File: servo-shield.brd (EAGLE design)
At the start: 65 x 56 mm, 31 parts, among them K1 PIN20X2

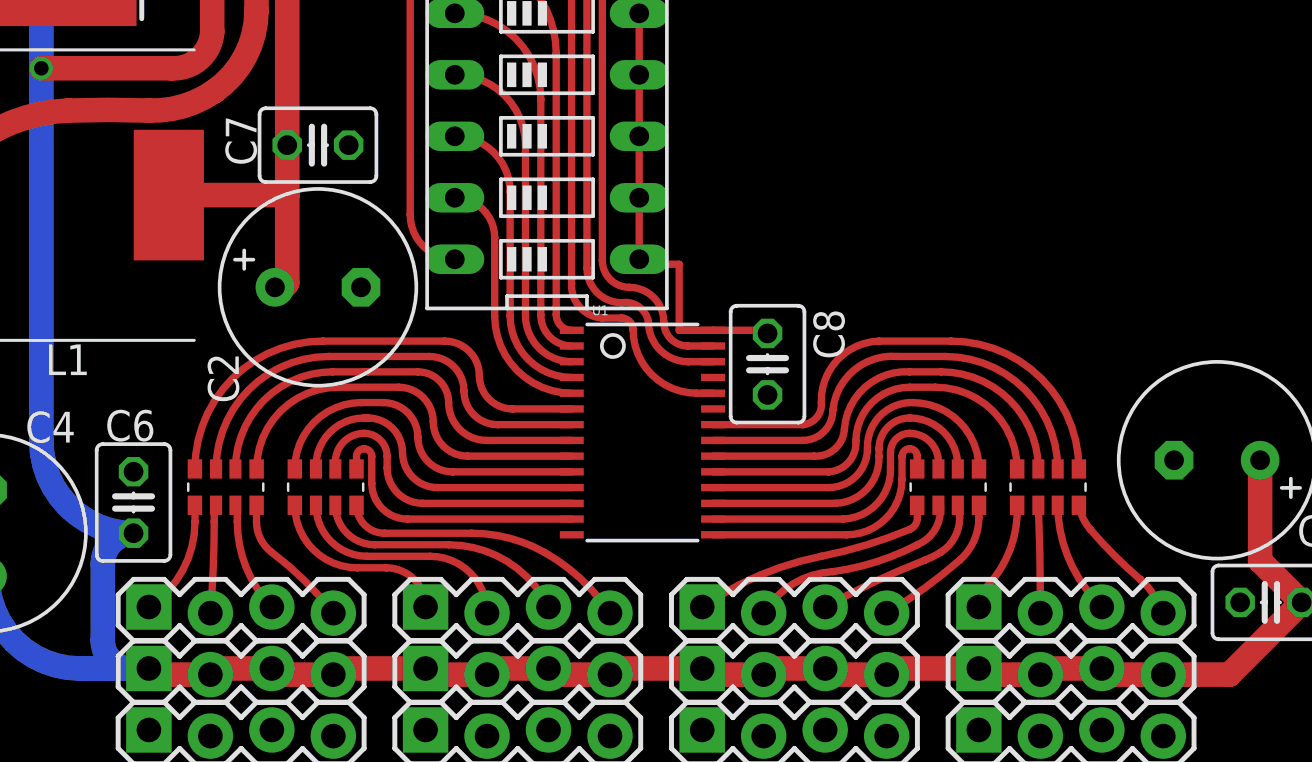
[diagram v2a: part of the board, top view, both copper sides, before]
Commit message: Rejig location of resistor networks
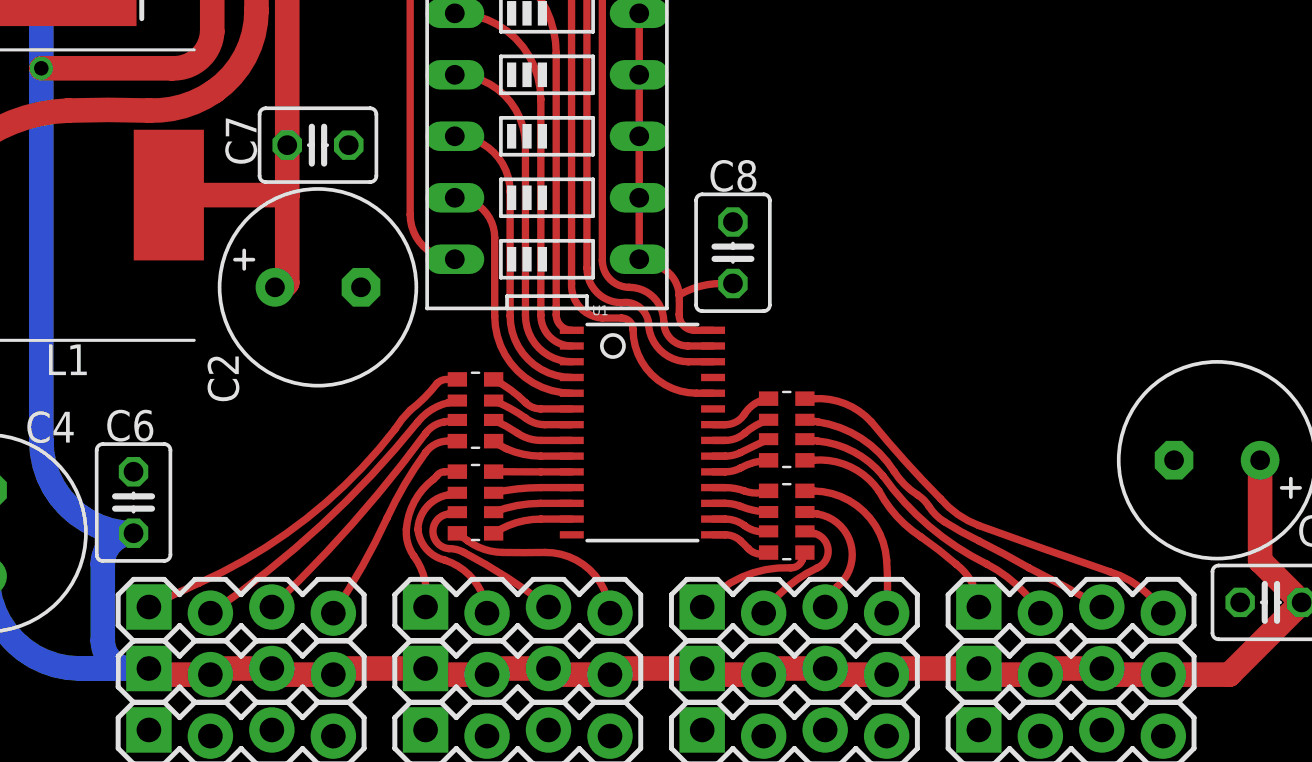
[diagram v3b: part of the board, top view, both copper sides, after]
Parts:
- moved RN1 11.1 mm to (37.8, 15.1), turned to 270 degrees
- moved RN4 10.8 mm to (24.9, 15.9), turned to 90 degrees
- moved RN2 6.82 mm to (37.8, 11.3), turned to 270 degrees
- moved RN3 6.22 mm to (24.9, 12.1), turned to 90 degrees
- moved C8 4.82 mm to (35.6, 22.4), turned to 90 degrees
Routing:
- net N$23: track 18.8 -> 2.59 mm
- net N$35: track 18.9 -> 3.59 mm
- net N$24: track 17.5 -> 2.49 mm
- net N$34: track 17.8 -> 3.46 mm
- net N$25: track 16.4 -> 2.44 mm
- net N$33: track 16.7 -> 3.42 mm
- net N$26: track 15.5 -> 2.36 mm
- net N$32: track 15.6 -> 3.35 mm
- net N$22: track 5.72 -> 17.7 mm
- net N$8: track 4.69 -> 16.0 mm
- net N$27: track 13.6 -> 2.31 mm
- net N$31: track 13.8 -> 3.23 mm
- net N$28: track 12.8 -> 2.33 mm
- net N$21: track 4.61 -> 14.6 mm
- net N$1: track 12.0 -> 2.37 mm
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
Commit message: Adding EagleCAD logo
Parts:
- added U$1: (no value), logo:EAGLE-PLC-8MM
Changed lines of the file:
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@@
 <attribute name="VALUE" x="13.843" y="9.779" size="1.27" layer="27" ratio="10" rot="R90"/>
 </element>
+<element name="U$1" library="logo" package="EAGLE-PLC-8MM" value="" x="40.16375" y="9.04875"/>
 </elements>
 <signals>

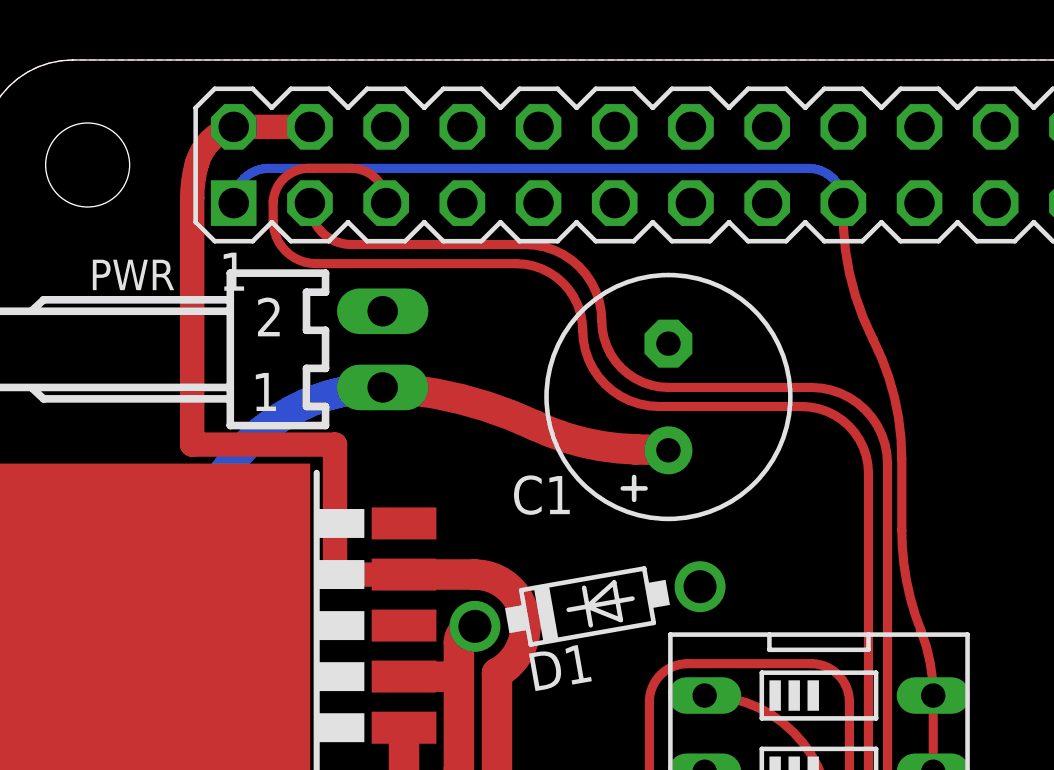
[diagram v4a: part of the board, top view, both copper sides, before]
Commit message: add jumper to select if RaspberryPi uses servo board regulator.
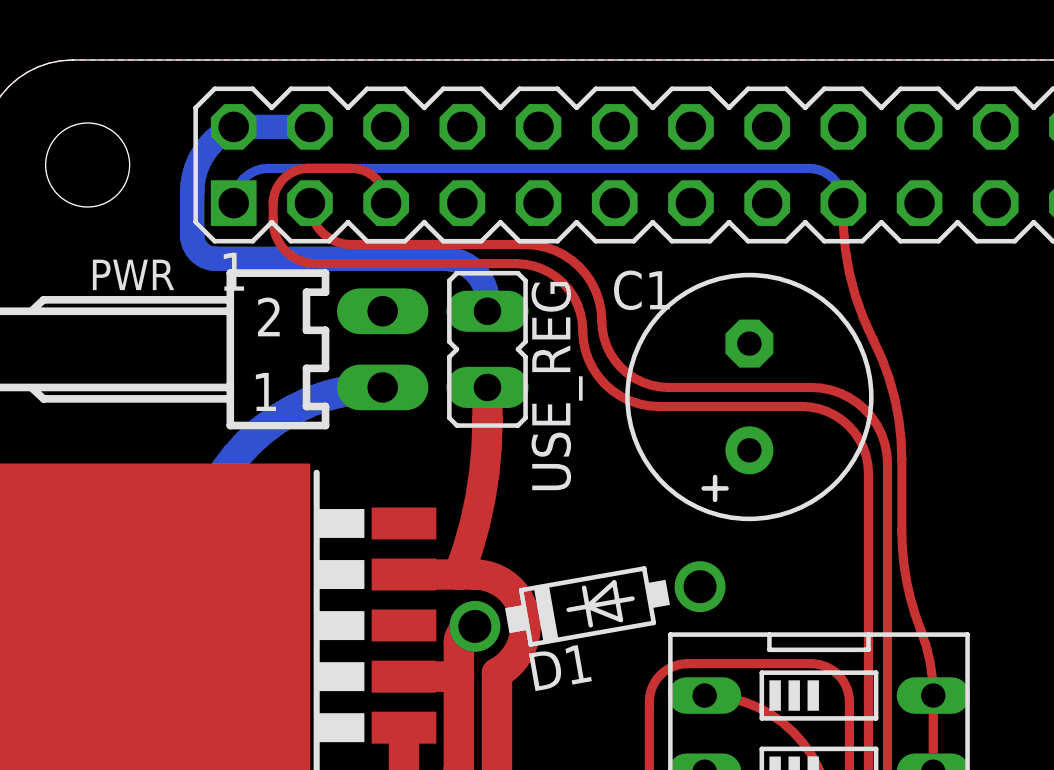
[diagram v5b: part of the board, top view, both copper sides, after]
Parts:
- added USE_REG: (no value), jumper:JP1
- moved C1 2.70 mm to (25.6, 44.8)
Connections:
- new net N$16: K1.2, K1.4, USE_REG.2
- net +5V: now also USE_REG.1; no longer K1.2, K1.4
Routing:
- net +5V: track 51.5 -> 32.8 mm
- net N$16: track 0.00 -> 17.6 mm
- net V+: track 130.9 -> 121.1 mm
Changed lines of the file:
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@@
 <attribute name="VALUE" x="16.129" y="23.78075" size="1.27" layer="27" ratio="10"/>
 </element>
-<element name="C1" library="rcl" package="E3,5-8" value="1000uf" x="22.86" y="44.7675" smashed="yes" rot="R90">
-<attribute name="NAME" x="19.71675" y="42.13225" size="1.27" layer="25" ratio="10" rot="R180"/>
-<attribute name="VALUE" x="25.908" y="42.4815" size="1.27" layer="27" ratio="10" rot="R90"/>
+<element name="C1" library="rcl" package="E3,5-8" value="1000uf" x="25.55875" y="44.7675" smashed="yes" rot="R90">
+<attribute name="NAME" x="23.0505" y="48.9585" size="1.27" layer="25" ratio="10" rot="R180"/>
+<attribute name="VALUE" x="28.60675" y="42.4815" size="1.27" layer="27" ratio="10" rot="R90"/>
 </element>
 <element name="C8" library="rcl" package="C025-030X050" value="100nf" x="35.56" y="22.38375" smashed="yes" rot="R90">
@@
 </element>
 <element name="U$1" library="logo" package="EAGLE-PLC-8MM" value="" x="40.16375" y="9.04875"/>
+<element name="USE_REG" library="jumper" package="JP1" value="" x="16.8275" y="46.355" smashed="yes">
+<attribute name="NAME" x="18.31975" y="48.73625" size="1.27" layer="25" ratio="10" rot="R270"/>
+<attribute name="VALUE" x="19.7485" y="43.815" size="1.27" layer="27" ratio="10" rot="R90"/>
+</element>
 </elements>
 <signals>
@@
 </signal>
 <signal name="+5V">
-<contactref element="K1" pad="2"/>
-<contactref element="K1" pad="4"/>
 <contactref element="IC2" pad="4"/>
 <contactref element="L1" pad="2"/>
@@
 <wire x1="17.145" y1="24.765" x2="17.145" y2="26.82875" width="1.016" layer="1"/>
 <wire x1="12.2525" y1="24.765" x2="17.145" y2="24.765" width="1.016" layer="1"/>
-<wire x1="14.0462" y1="38.8493" x2="11.7475" y2="38.8493" width="0.8128" layer="1"/>
-<wire x1="11.7475" y1="38.8493" x2="11.7475" y2="43.18" width="0.8128" layer="1"/>
-<wire x1="11.7475" y1="43.18" x2="6.985" y2="43.18" width="0.8128" layer="1"/>
-<wire x1="6.985" y1="43.18" x2="6.985" y2="51.38875" width="0.8128" layer="1"/>
-<wire x1="10.91" y1="53.77" x2="8.37" y2="53.77" width="0.8128" layer="1"/>
-<wire x1="14.0462" y1="38.8493" x2="16.3957" y2="38.8493" width="1.016" layer="1"/>
+<wire x1="14.0462" y1="38.8493" x2="15.875" y2="38.8493" width="1.016" layer="1"/>
+<wire x1="15.875" y1="38.8493" x2="16.3957" y2="38.8493" width="1.016" layer="1"/>
 <wire x1="16.3957" y1="38.8493" x2="18.0975" y2="37.1475" width="1.016" layer="1" curve="-90"/>
 <wire x1="18.0975" y1="37.1475" x2="17.145" y2="35.56" width="1.016" layer="1" curve="-61.927542"/>
 <wire x1="17.145" y1="35.56" x2="17.145" y2="26.82875" width="1.016" layer="1"/>
-<wire x1="6.985" y1="51.38875" x2="7.14375" y2="52.54625" width="0.8128" layer="1" curve="-15.618678"/>
-<wire x1="7.14375" y1="52.54625" x2="8.37" y2="53.77" width="0.8128" layer="1" curve="-58.879556"/>
+<contactref element="USE_REG" pad="1"/>
+<wire x1="16.8275" y1="45.085" x2="16.8275" y2="43.97375" width="1.016" layer="1"/>
+<wire x1="16.8275" y1="43.97375" x2="15.875" y2="38.8493" width="1.016" layer="1" curve="-21.059214"/>
 </signal>
 <signal name="ID_SCL">
@@
 <wire x1="12.3825" y1="30.00375" x2="6.985" y2="30.00375" width="1.016" layer="1"/>
 <via x="6.985" y="30.00375" extent="1-16" drill="0.6" shape="square"/>
-<wire x1="22.86" y1="42.9895" x2="21.74875" y2="43.02125" width="1.016" layer="1"/>
-<wire x1="21.74875" y1="43.02125" x2="18.415" y2="43.815" width="1.016" layer="1" curve="-23.511764"/>
-<wire x1="18.415" y1="43.815" x2="13.335" y2="45.085" width="1.016" layer="1" curve="22.224253"/>
 <wire x1="25.4" y1="4.953" x2="22.86" y2="4.953" width="1.016" layer="1"/>
 <wire x1="22.86" y1="4.953" x2="22.86" y2="5.207" width="1.016" layer="1"/>
+<wire x1="13.335" y1="45.085" x2="25.55875" y2="42.9895" width="0" layer="19" extent="1-1"/>
 </signal>
 <signal name="VOUT">
@@
 <wire x1="26.3525" y1="24.91" x2="26.3525" y2="19.7797" width="0.3048" layer="1"/>
 </signal>
+<signal name="N$16">
+<contactref element="K1" pad="2"/>
+<contactref element="K1" pad="4"/>
+<contactref element="USE_REG" pad="2"/>
+<wire x1="8.37" y1="53.77" x2="10.91" y2="53.77" width="0.8128" layer="16"/>
+<wire x1="16.8275" y1="47.625" x2="16.8275" y2="47.9425" width="0.8128" layer="16"/>
+<wire x1="16.8275" y1="47.9425" x2="15.39875" y2="49.37125" width="0.8128" layer="16" curve="90"/>
+<wire x1="15.39875" y1="49.37125" x2="7.77875" y2="49.37125" width="0.8128" layer="16"/>
+<wire x1="7.77875" y1="49.37125" x2="6.985" y2="50.165" width="0.8128" layer="16" curve="-90"/>
+<wire x1="6.985" y1="50.165" x2="6.985" y2="51.59375" width="0.8128" layer="16"/>
+<wire x1="6.985" y1="51.59375" x2="8.37" y2="53.77" width="0.8128" layer="16" curve="-64.946612"/>
+</signal>
 </signals>

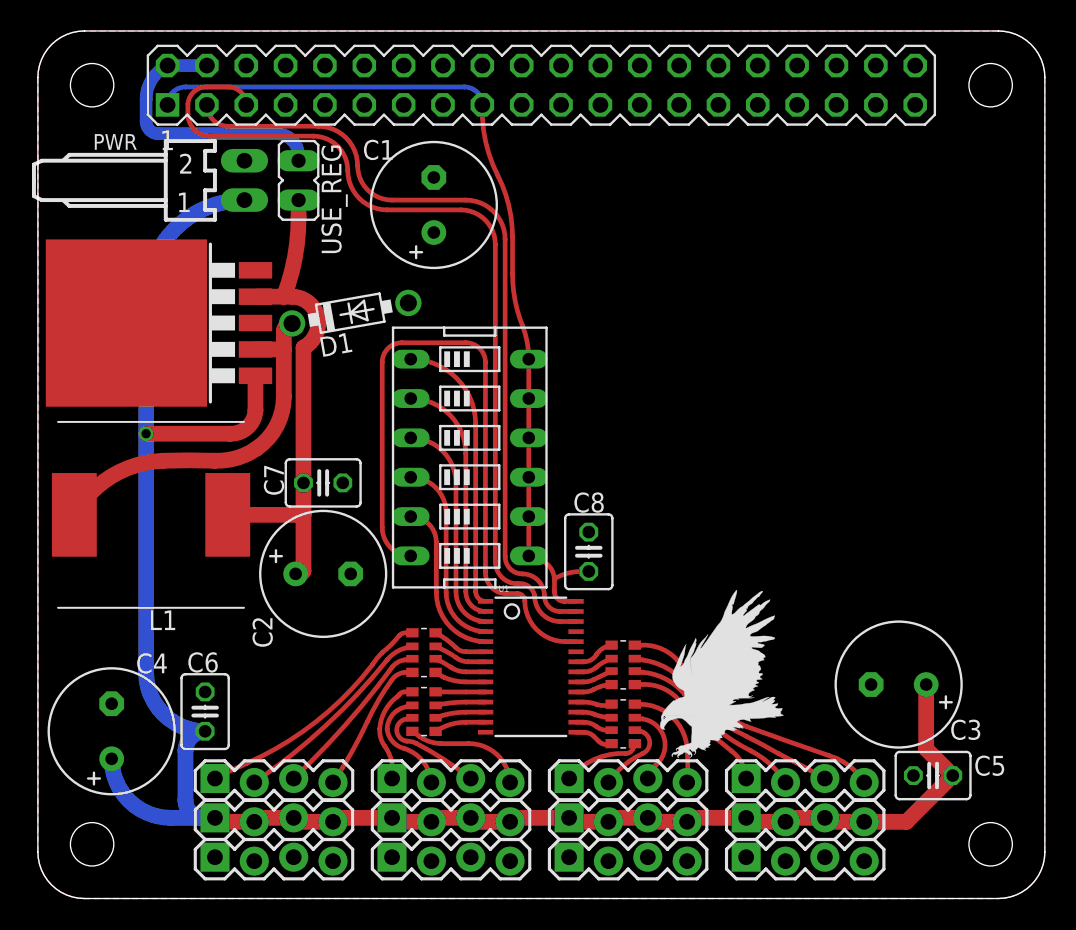
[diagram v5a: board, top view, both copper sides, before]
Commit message: Rejigged to add passthru power connector
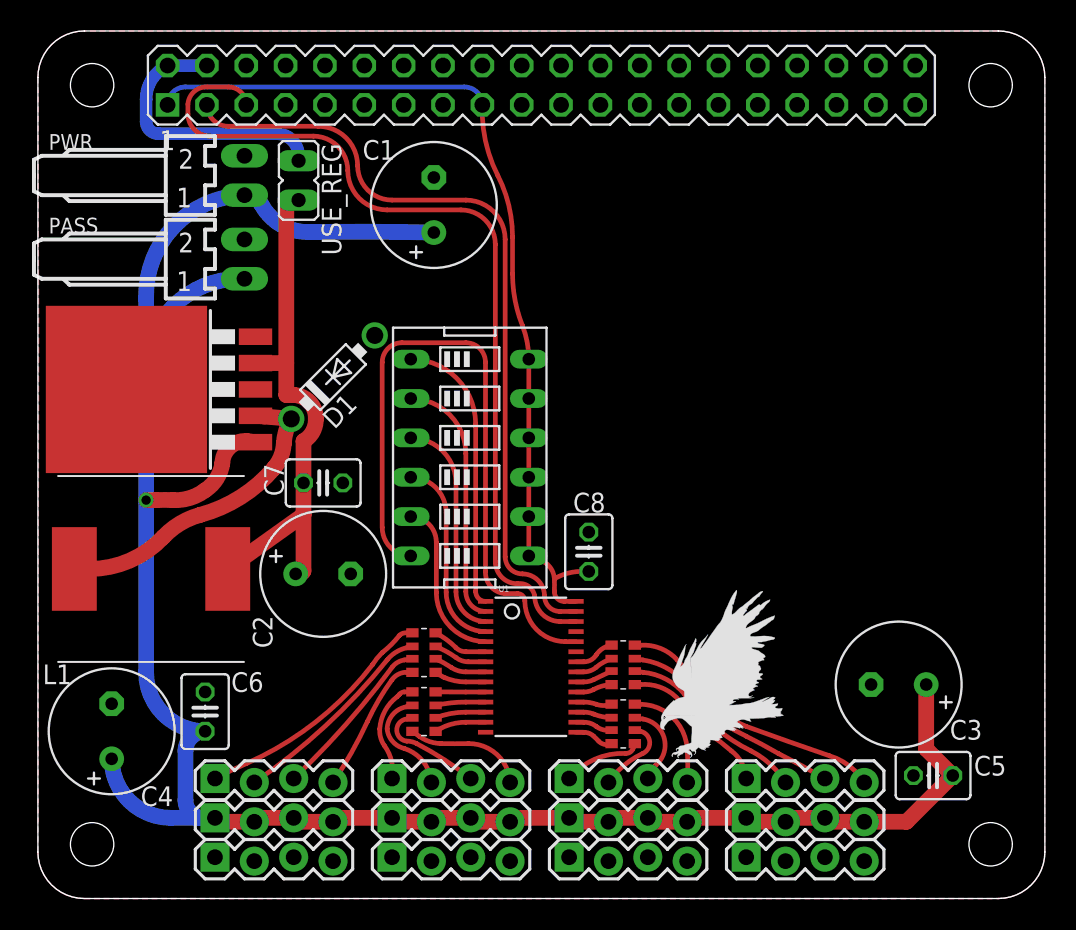
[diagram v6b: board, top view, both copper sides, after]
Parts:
- added PASS: 22-05-7028-02, con-molex:7395-02
- moved IC2 4.29 mm to (8.26, 32.9)
- moved D1 4.27 mm to (19.1, 33.7), turned to 45 degrees
- moved L1 3.49 mm to (7.30, 21.3)
- moved PWR 0.32 mm to (13.3, 46.7)
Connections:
- net GND: now also PASS.2
- net V+: now also PASS.1
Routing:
- net V+: track 121.1 -> 141.9 mm
- net VOUT: track 23.4 -> 20.3 mm
- net +5V: track 32.8 -> 34.5 mm
